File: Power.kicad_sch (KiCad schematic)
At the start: 0 parts

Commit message: PMIC DCDC
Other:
- title: Leaf RV1126 Power -> Leaf RV1126 PMIC RK809
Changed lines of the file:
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@@
   (paper "A4")
   (title_block
-    (title "Leaf RV1126 Power")
+    (title "Leaf RV1126 PMIC RK809")
     (date "2023-02-23")
     (rev "1")

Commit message: updated: PMIC codec
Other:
- title: Leaf RV1126 PMIC RK809 -> Leaf RV1126 PMIC RK809 Codec
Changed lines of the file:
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@@
   (paper "A4")
   (title_block
-    (title "Leaf RV1126 PMIC RK809")
-    (date "2023-02-23")
+    (title "Leaf RV1126 PMIC RK809 Codec")
+    (date "2023-02-25")
     (rev "1")
     (company "Qingdao IotPi Information Technology")

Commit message: updated: titles
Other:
- title: Leaf RV1126 PMIC RK809 Codec -> Leaf RV1126 Power
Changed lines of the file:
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@@
   (paper "A4")
   (title_block
-    (title "Leaf RV1126 PMIC RK809 Codec")
+    (title "Leaf RV1126 Power")
     (date "2023-02-25")
     (rev "1")

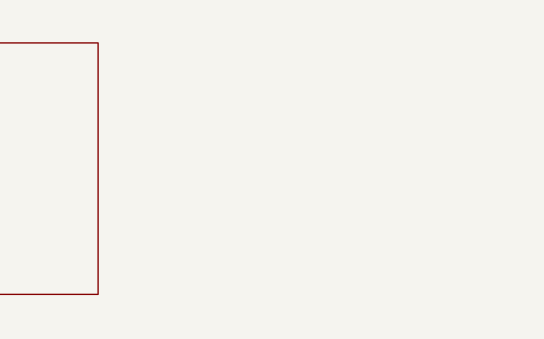
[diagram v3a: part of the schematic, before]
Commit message: fix some ERCs
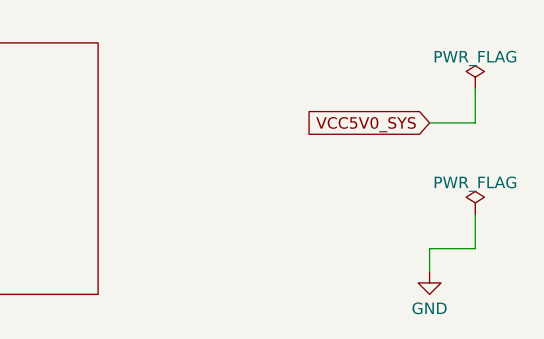
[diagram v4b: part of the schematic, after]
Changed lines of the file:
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@@
     (company "Qingdao IotPi Information Technology")
+  )
+  (wire (pts (xy 180.34 48.26) (xy 185.42 48.26))
+    (stroke (width 0) (type default))
+  )
+  (wire (pts (xy 180.34 62.23) (xy 180.34 64.77))
+    (stroke (width 0) (type default))
+  )
+  (wire (pts (xy 185.42 48.26) (xy 185.42 44.45))
+    (stroke (width 0) (type default))
+  )
+  (wire (pts (xy 180.34 62.23) (xy 185.42 62.23))
+    (stroke (width 0) (type default))
+  )
+  (wire (pts (xy 185.42 62.23) (xy 185.42 58.42))
+    (stroke (width 0) (type default))
+  )
+  (global_label "VCC5V0_SYS" (shape input) (at 180.34 48.26 180) (fields_autoplaced)
+    (effects (font (size 1.27 1.27)) (justify right))
+    (property "Intersheetrefs" "${INTERSHEET_REFS}" (at 165.8228 48.26 0)
+      (effects (font (size 1.27 1.27)) (justify right) hide)
+    )
+  )
+  (symbol (lib_id "power:GND") (at 180.34 64.77 0) (unit 1)
+    (in_bom yes) (on_board yes) (dnp no) (fields_autoplaced)
+    (property "Reference" "#PWR0143" (at 180.34 71.12 0)
+      (effects (font (size 1.27 1.27)) hide)
+    )
+    (property "Value" "GND" (at 180.34 68.9055 0)
+      (effects (font (size 1.27 1.27)))
+    )
+    (property "Footprint" "" (at 180.34 64.77 0)
+      (effects (font (size 1.27 1.27)) hide)
+    )
+    (property "Datasheet" "" (at 180.34 64.77 0)
+      (effects (font (size 1.27 1.27)) hide)
+    )
+    (pin "1")
+    (instances
+      (project "leaf"
+        (path "/e3b58043-16a3-43c8-9fad-9c9784eebfa4/cc9fb3ac-19c3-47a8-ba7d-678b4d514ff0"
+          (reference "#PWR0143") (unit 1)
+        )
+      )
+    )
+  )
+  (symbol (lib_id "power:PWR_FLAG") (at 185.42 44.45 0) (unit 1)
+    (in_bom yes) (on_board yes) (dnp no) (fields_autoplaced)
+    (property "Reference" "#FLG01" (at 185.42 42.545 0)
+      (effects (font (size 1.27 1.27)) hide)
+    )
+    (property "Value" "PWR_FLAG" (at 185.42 40.9481 0)
+      (effects (font (size 1.27 1.27)))
+    )
+    (property "Footprint" "" (at 185.42 44.45 0)
+      (effects (font (size 1.27 1.27)) hide)
+    )
+    (property "Datasheet" "~" (at 185.42 44.45 0)
+      (effects (font (size 1.27 1.27)) hide)
+    )
+    (pin "1")
+    (instances
+      (project "leaf"
+        (path "/e3b58043-16a3-43c8-9fad-9c9784eebfa4/cc9fb3ac-19c3-47a8-ba7d-678b4d514ff0"
+          (reference "#FLG01") (unit 1)
+        )
+      )
+    )
+  )
+  (symbol (lib_id "power:PWR_FLAG") (at 185.42 58.42 0) (unit 1)
+    (in_bom yes) (on_board yes) (dnp no) (fields_autoplaced)
+    (property "Reference" "#FLG02" (at 185.42 56.515 0)
+      (effects (font (size 1.27 1.27)) hide)
+    )
+    (property "Value" "PWR_FLAG" (at 185.42 54.9181 0)
+      (effects (font (size 1.27 1.27)))
+    )
+    (property "Footprint" "" (at 185.42 58.42 0)
+      (effects (font (size 1.27 1.27)) hide)
+    )
+    (property "Datasheet" "~" (at 185.42 58.42 0)
+      (effects (font (size 1.27 1.27)) hide)
+    )
+    (pin "1")
+    (instances
+      (project "leaf"
+        (path "/e3b58043-16a3-43c8-9fad-9c9784eebfa4/cc9fb3ac-19c3-47a8-ba7d-678b4d514ff0"
+          (reference "#FLG02") (unit 1)
+        )
+      )
+    )
   )
   (sheet (at 101.6 39.37) (size 41.91 27.94) (fields_autoplaced)

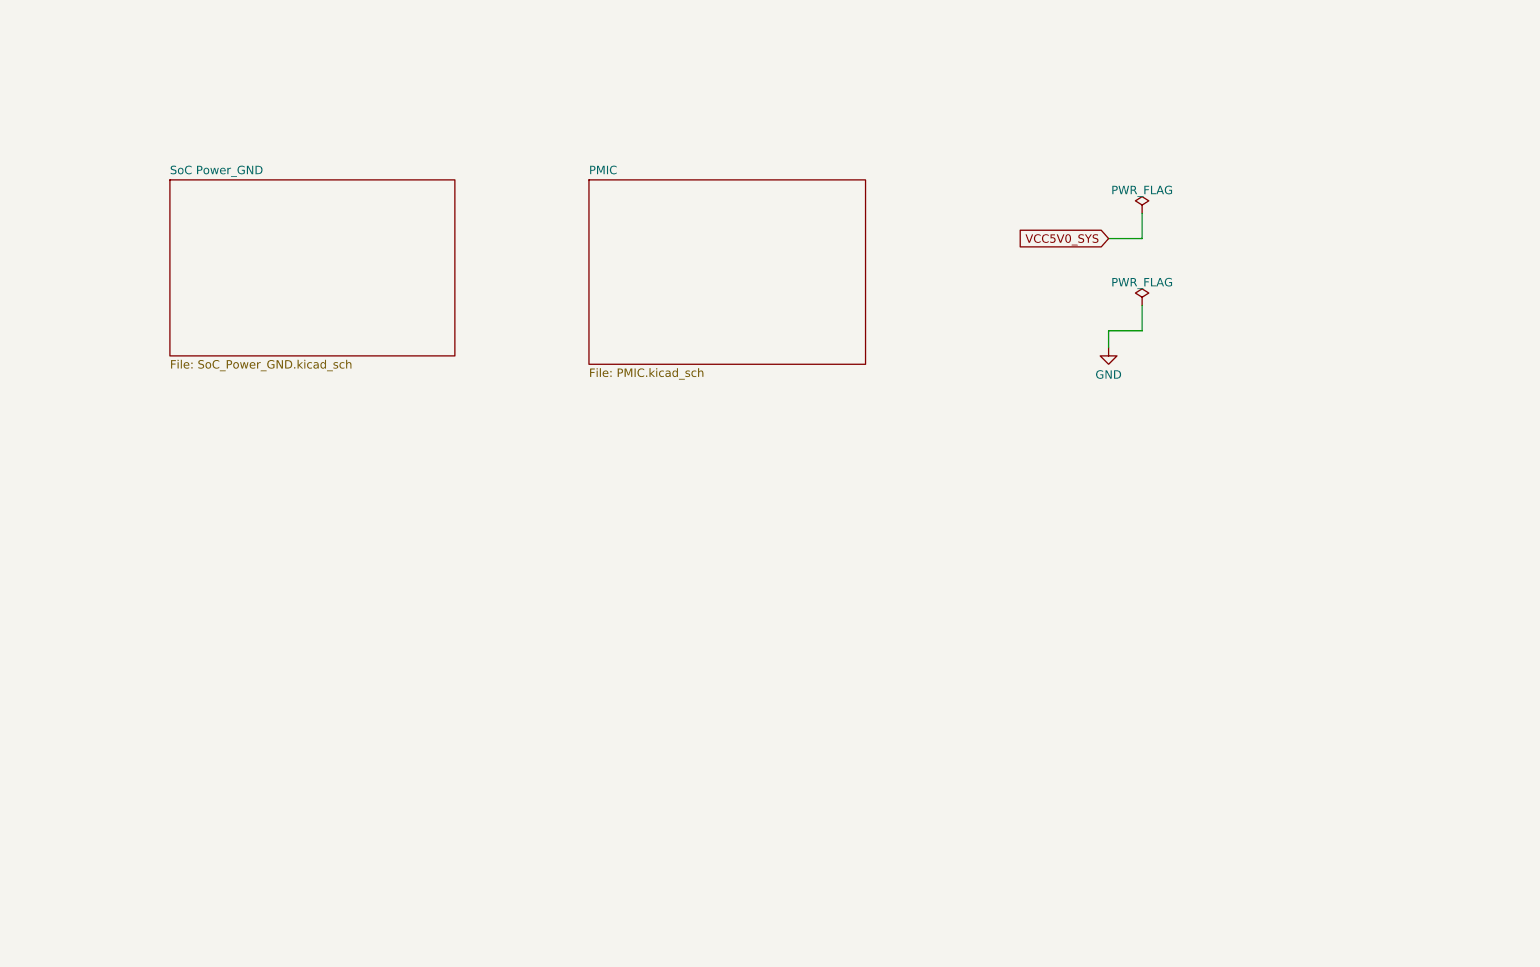
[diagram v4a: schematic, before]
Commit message: added VDD Logic
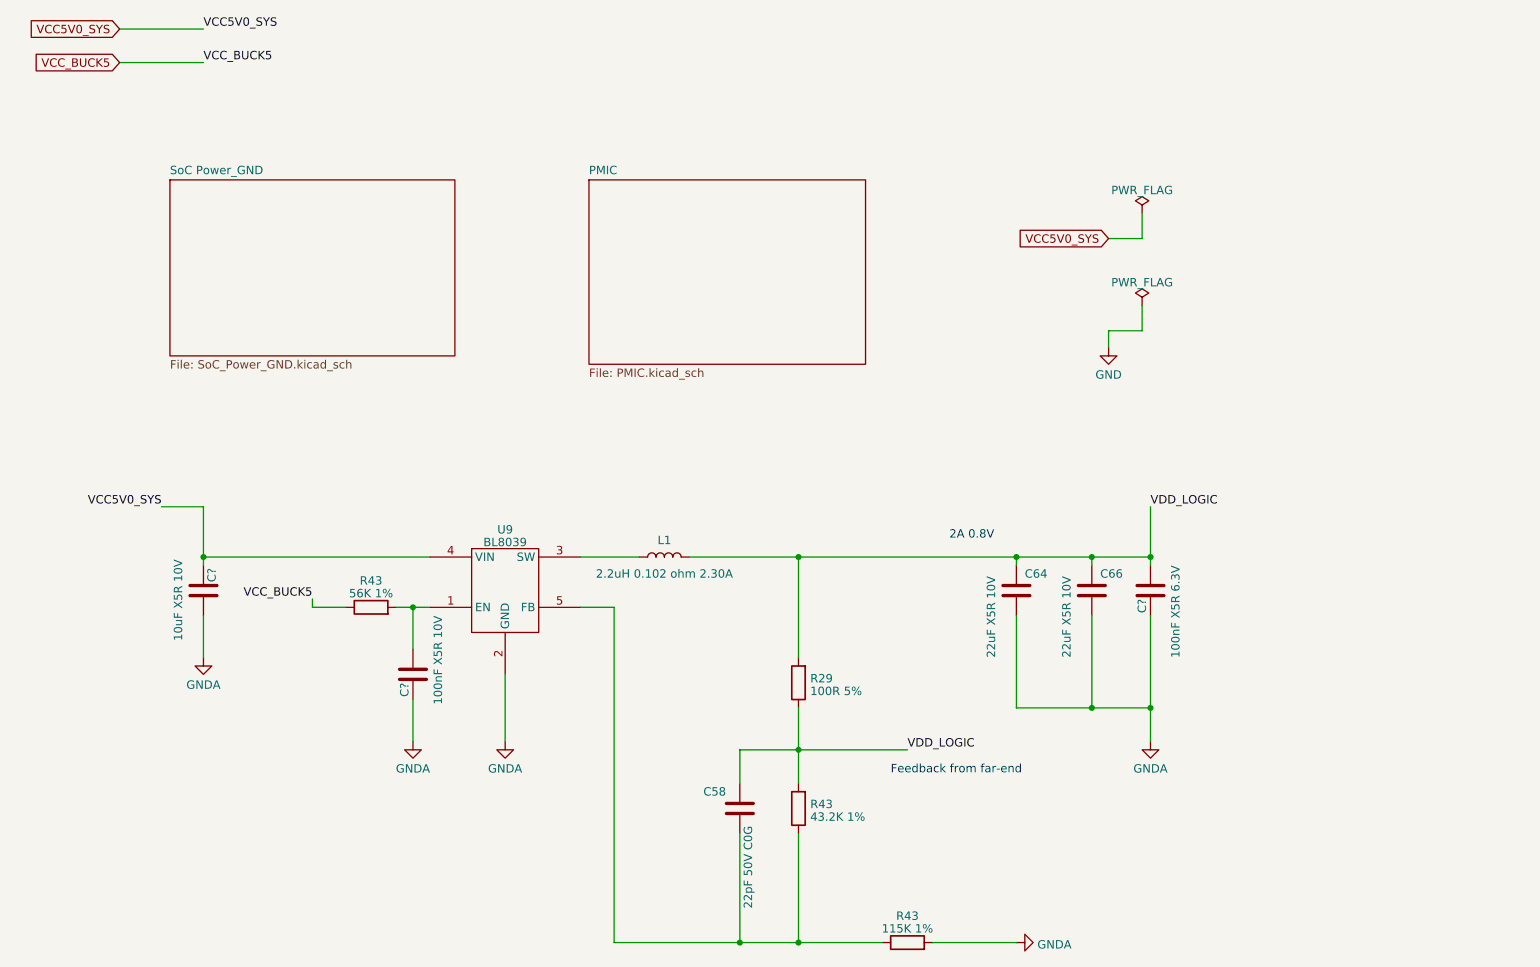
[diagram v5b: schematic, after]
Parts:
- added C58: 22pF 50V C0G, Capacitor_SMD:C_0201_0603Metric, symbol Device:C
- added C64, C66: 22uF X5R 10V, Resistor_SMD:R_0603_1608Metric, symbol Device:C
- added C?: 100nF X5R 10V, Capacitor_SMD:C_0402_1005Metric, symbol Device:C
- added C?: 100nF X5R 6.3V, Capacitor_SMD:C_0201_0603Metric, symbol Device:C
- added C?: 10uF X5R 10V, Capacitor_SMD:C_0402_1005Metric, symbol Device:C
- added L1: 2.2uH 0.102 ohm 2.30A, Inductor_SMD:L_0805_2012Metric, symbol Device:L
- added R29: 100R 5%, Resistor_SMD:R_0402_1005Metric, symbol Device:R
- added R43: 43.2K 1%, Resistor_SMD:R_0402_1005Metric, symbol Device:R
- added R43: 56K 1%, Resistor_SMD:R_0402_1005Metric, symbol Device:R
- added R43: 115K 1%, Resistor_SMD:R_0402_1005Metric, symbol Device:R
- added U9: BL8039, Package_TO_SOT_SMD:SOT-23-5_HandSoldering, symbol Leaf_Converter_DCDC:BL8039
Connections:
- net VCC5V0_SYS: now also C?.1, U9.4 (VIN)
- new net: C?.2, R43.2, U9.1 (EN)
- new net: L1.1, U9.3 (SW)
- new net: C58.2, R43.1, R43.1, U9.5 (FB)
- new net GNDA: C64.2, C66.2, C?.1, C?.1, C?.2, R43.2, U9.2 (GND)
- new net VCC_BUCK5: R43.1
- new net VDD_LOGIC: C58.1, C64.1, C66.1, C?.2, L1.2, R29.1, R29.2, R43.2
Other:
- note added: "2A 0.8V"
- note added: "Feedback from far-end"

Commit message: updated for ERC
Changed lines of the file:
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@@
+    (stroke (width 0) (type default))
+  )
+  (wire (pts (xy 177.8 91.44) (xy 177.8 96.52))
     (stroke (width 0) (type default))
   )
@@
   )
   (wire (pts (xy 36.83 88.9) (xy 43.18 88.9))
+    (stroke (width 0) (type default))
+  )
+  (wire (pts (xy 30.48 26.67) (xy 43.18 26.67))
     (stroke (width 0) (type default))
   )
@@
   (label "VCC_BUCK5" (at 59.69 102.87 180) (fields_autoplaced)
     (effects (font (size 1.27 1.27)) (justify right bottom))
+  )
+  (label "VDD_LOGIC" (at 43.18 26.67 0) (fields_autoplaced)
+    (effects (font (size 1.27 1.27)) (justify left bottom))
   )
   (global_label "VCC_BUCK5" (shape input) (at 30.48 21.59 180) (fields_autoplaced)
@@
     )
   )
+  (global_label "VDD_LOGIC" (shape output) (at 30.48 26.67 180) (fields_autoplaced)
+    (effects (font (size 1.27 1.27)) (justify right))
+    (property "Intersheetrefs" "${INTERSHEET_REFS}" (at 17.4746 26.67 0)
+      (effects (font (size 1.27 1.27)) (justify right) hide)
+    )
+  )
   (global_label "VCC5V0_SYS" (shape input) (at 30.48 16.51 180) (fields_autoplaced)
     (effects (font (size 1.27 1.27)) (justify right))
@@
         )
       )
+    )
+  )
+  (symbol (lib_id "power:PWR_FLAG") (at 177.8 91.44 0) (unit 1)
+    (in_bom yes) (on_board yes) (dnp no) (fields_autoplaced)
+    (property "Reference" "#FLG012" (at 177.8 89.535 0)
+      (effects (font (size 1.27 1.27)) hide)
+    )
+    (property "Value" "PWR_FLAG" (at 177.8 87.9381 0)
+      (effects (font (size 1.27 1.27)))
+    )
+    (property "Footprint" "" (at 177.8 91.44 0)
+      (effects (font (size 1.27 1.27)) hide)
+    )
+    (property "Datasheet" "~" (at 177.8 91.44 0)
+      (effects (font (size 1.27 1.27)) hide)
+    )
+    (pin "1")
+    (instances
+      (project "leaf"
+        (path "/e3b58043-16a3-43c8-9fad-9c9784eebfa4/cc9fb3ac-19c3-47a8-ba7d-678b4d514ff0"
+          (reference "#FLG012") (unit 1)
+        )
+      )

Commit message: updated symbols
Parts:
- added NT1: NetTie_3_Tee, symbol Device:NetTie_3_Tee
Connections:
- net GND: now also NT1.2
- net GNDA: now also NT1.1
- new net GNDD: NT1.3
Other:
- sheet PMIC ports: added I2C_SCL, I2C_SDA, INT, RESET, SLEEP; removed none

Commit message: fix errors
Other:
- sheet PMIC ports: added CLK_32K; removed none
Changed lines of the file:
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@@
+    (stroke (width 0) (type default))
+  )
+  (wire (pts (xy 81.28 29.21) (xy 87.63 29.21))
     (stroke (width 0) (type default))
   )
@@
     (stroke (width 0) (type default))
   )
+  (wire (pts (xy 101.6 63.5) (xy 95.25 63.5))
+    (stroke (width 0) (type default))
+  )
   (wire (pts (xy 133.35 96.52) (xy 166.37 96.52))
     (stroke (width 0) (type default))
@@
     (stroke (width 0) (type default))
   )
-  (wire (pts (xy 96.52 59.69) (xy 101.6 59.69))
+  (wire (pts (xy 95.25 59.69) (xy 101.6 59.69))
     (stroke (width 0) (type default))
   )
@@
     (stroke (width 0) (type default))
   )
+  (wire (pts (xy 101.6 50.8) (xy 95.25 50.8))
+    (stroke (width 0) (type default))
+  )
   (wire (pts (xy 59.69 102.87) (xy 59.69 104.14))
     (stroke (width 0) (type default))
@@
   (label "PMIC_INT" (at 87.63 16.51 0) (fields_autoplaced)
     (effects (font (size 1.27 1.27)) (justify left bottom))
+  )
+  (label "PMIC_RESET" (at 95.25 63.5 180) (fields_autoplaced)
+    (effects (font (size 1.27 1.27)) (justify right bottom))
   )
   (label "PMIC_I2C_SCL" (at 95.25 44.45 180) (fields_autoplaced)
@@
     (effects (font (size 1.27 1.27)) (justify left bottom))
   )
+  (label "PMIC_CLK32K" (at 87.63 29.21 0) (fields_autoplaced)
+    (effects (font (size 1.27 1.27)) (justify left bottom))
+  )
   (label "VCC_BUCK5" (at 43.18 21.59 0) (fields_autoplaced)
     (effects (font (size 1.27 1.27)) (justify left bottom))
@@
     (effects (font (size 1.27 1.27)) (justify left bottom))
   )
-  (label "PMIC_SLEEP" (at 96.52 59.69 180) (fields_autoplaced)
+  (label "PMIC_SLEEP" (at 95.25 59.69 180) (fields_autoplaced)
     (effects (font (size 1.27 1.27)) (justify right bottom))
   )
@@
   (label "PMIC_I2C_SCL" (at 87.63 21.59 0) (fields_autoplaced)
     (effects (font (size 1.27 1.27)) (justify left bottom))
+  )
+  (label "PMIC_CLK32K" (at 95.25 50.8 180) (fields_autoplaced)
+    (effects (font (size 1.27 1.27)) (justify right bottom))
   )
   (global_label "VCC_BUCK5" (shape input) (at 30.48 21.59 180) (fields_autoplaced)
@@
       (effects (font (size 1.27 1.27)) (justify right) hide)
     )
+  )
+  (hierarchical_label "PMIC_CLK32K" (shape output) (at 81.28 29.21 180) (fields_autoplaced)
+    (effects (font (size 1.27 1.27)) (justify right))
   )
   (hierarchical_label "PMIC_SLEEP" (shape output) (at 81.28 19.05 180) (fields_autoplaced)
@@
       (effects (font (size 1.27 1.27)) (justify left))
     )
+    (pin "CLK_32K" output (at 101.6 50.8 180)
+      (effects (font (size 1.27 1.27)) (justify left))
+    )
